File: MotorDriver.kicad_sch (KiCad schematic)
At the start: 93 parts, among them J1 Screw_Terminal_01x02, J2 Screw_Terminal_01x02, J3 Screw_Terminal_01x02, J4 Conn_01x07_Pin, J5 Conn_01x05_Pin, Q1 PMOS, U1 L298N, U2 INA226, U3 INA226, U4 INA226, U5 AP63205WU, U6 LM393, U7 AP2112K-3.3

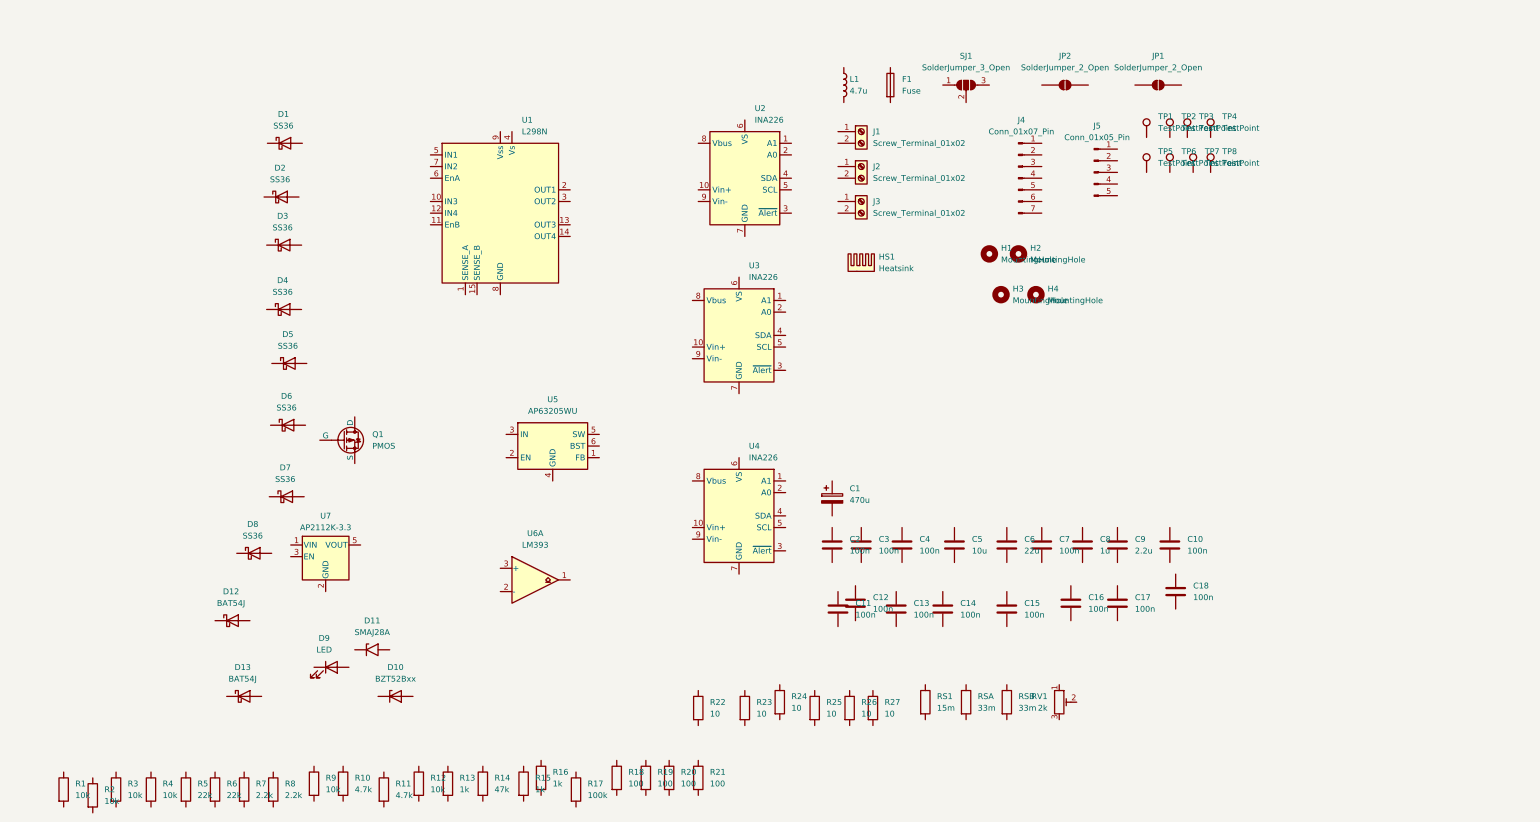
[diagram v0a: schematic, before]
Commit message: schematic update
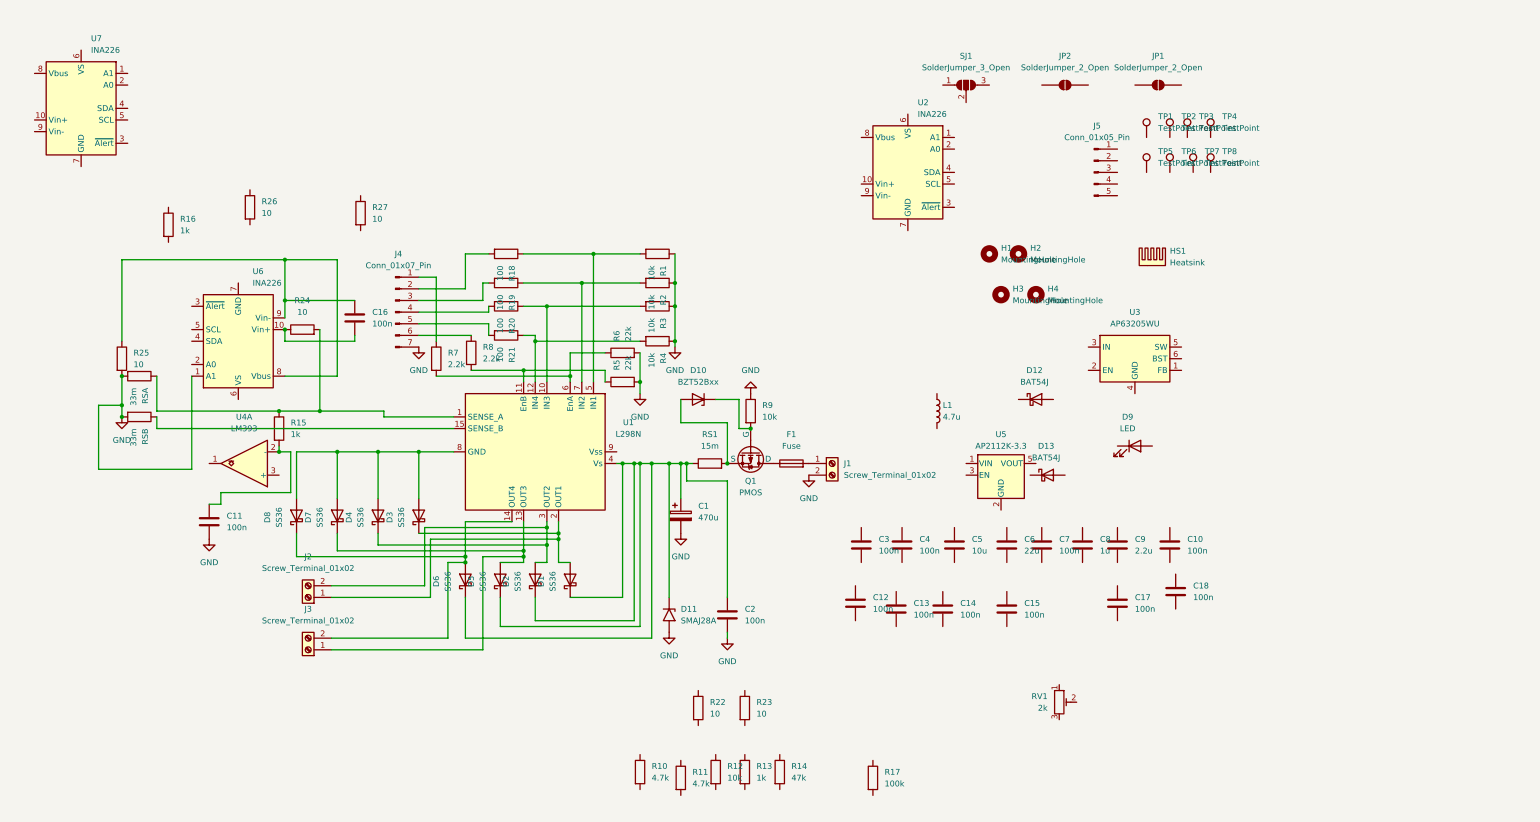
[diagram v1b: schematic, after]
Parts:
- renumbered U5 to U3, U6 to U4, U7 to U5, U4 to U6, U3 to U7
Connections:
- net at R20.1: now also R3.2, U1.10 (IN3)
- net at R20.2: now also J4.4 (Pin_4)
- net at J4.1 (Pin_1): now also R7.1
- net at J4.2 (Pin_2): now also R18.2
- net at J4.3 (Pin_3): now also R19.2
- net at J4.5 (Pin_5): now also R21.2
- net at J4.6 (Pin_6): now also R8.1
- net GND: now reaches J4.7 (Pin_7)
- net GND: now also C1.2, C11.2, C2.2, D11.2 (A2), J1.2 (Pin_2), R1.1, R2.1, R25.2, R3.1, R4.1, R5.2, R6.2, R9.1, RSA.2, RSB.2, U6.1 (A1)
- net at D10.1 (K): now also Q1.2 (G), R9.2
- net at D10.2 (A): now also Q1.3 (S), RS1.2
- net at C1.1: now also C2.1, D1.1 (K), D11.1 (A1), D2.1 (K), D5.1 (K), D6.1 (K), RS1.1, U1.4 (Vs)
- net at R8.2: now also R5.1, U1.11 (EnB)
- net at U1.1 (SENSE_A): now also R15.1, R24.2, RSA.1
- net at U1.12 (IN4): now also R21.1, R4.2
- net at U1.13 (OUT3): now also D5.2 (A), D7.1 (K), J3.1 (Pin_1)
- net at U1.14 (OUT4): now also D6.2 (A), D8.1 (K), J3.2 (Pin_2)
- net at U1.15 (SENSE_B): now also RSB.1
- net at U1.2 (OUT1): now also D1.2 (A), D3.1 (K), J2.1 (Pin_1)
- net at U1.3 (OUT2): now also D2.2 (A), D4.1 (K), J2.2 (Pin_2)
- net at U1.5 (IN1): now also R1.2, R18.1
- net at U1.6 (EnA): now also R6.1, R7.2
- net at U1.7 (IN2): now also R19.1, R2.2
- net at U1.8 (GND): now also D3.2 (A), D4.2 (A), D7.2 (A), D8.2 (A)
- net at U6.10 (Vin+): now also C16.2, R24.1
- net at U6.8 (Vbus): now also C16.1, R25.1, U6.9 (Vin-)
- net at Q1.1 (D): now also F1.1
- net at J1.1 (Pin_1): now also F1.2
- net at C11.1: now also R15.2, U4.2 (-)
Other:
- moved on the sheet: C1, C11, C16, C2, D1, D10, D12, D13, D5, D6, D7, D8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

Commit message: final schematic
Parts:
- removed JP1, JP2: SolderJumper_2_Open, symbol Jumper:SolderJumper_2_Open
- added JP1, JP2: SolderJumper_2_Bridged, symbol Jumper:SolderJumper_2_Bridged
- added unit 2 of U4
- added unit 3 of U4
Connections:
- net GND: now also C10.2, C12.2, C13.1, C15.2, C17.2, C3.2, C4.2, C5.2, C6.2, C8.1, C9.2, D9.1 (K), J5.5 (Pin_5), R27.2, RV1.3, TP2.1, U2.1 (A1), U2.2 (A0), U2.7 (GND), U3.4 (GND), U5.2 (GND), U6.7 (GND), U7.1 (A1), U7.7 (GND), U4.4 (V-)
- net at C12.1: now also R16.2, U4.6 (-)
- net at C18.1: now also R27.1, U7.8 (Vbus), U7.9 (Vin-)
- net at C18.2: now also R26.1, U7.10 (Vin+)
- net at U2.10 (Vin+): now also C14.1, R22.1
- net at U2.3 (~{Alert}): now also J5.3 (Pin_3), R12.1, U6.3 (~{Alert}), U7.3 (~{Alert})
- net at U2.4 (SDA): now also C16.1, J5.1 (Pin_1), R25.1, U6.4 (SDA), U6.8 (Vbus), U6.9 (Vin-), U7.2 (A0), U7.4 (SDA), JP1.1 (A)
- net at U2.5 (SCL): now also J5.2 (Pin_2), U6.5 (SCL), U7.5 (SCL), JP2.1 (A)
- net at U2.6 (VS): now also C10.1, C15.1, C17.1, C4.1, J5.4 (Pin_4), R10.2, R11.2, R12.2, SJ1.2 (C), U6.2 (A0), U6.6 (VS), U7.6 (VS), U4.8 (V+)
- net at U2.8 (Vbus): now also C1.1, C2.1, C5.1, D1.1 (K), D11.1 (A1), D2.1 (K), D5.1 (K), D6.1 (K), R17.1, R23.1, RS1.1, TP1.1, U1.4 (Vs), U3.3 (IN)
- net at U2.9 (Vin-): now also C14.2, R23.2
- net at D10.2 (A), Q1.3 (S), RS1.2: now also R22.2
- net at R5.1, R8.2, U1.11 (EnB): now also D13.1 (K)
- net at R15.1, R24.2, RSA.1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: now also TP5.1
- net at D5.2 (A), D7.1 (K), J3.1 (Pin_1)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: now also D2.2 (A), D4.1 (K), J2.2 (Pin_2), TP8.1, U1.3 (OUT2)
- net at RSB.1, U1.15 (SENSE_B): now also R16.1, R26.2, TP6.1
- net at D1.2 (A), D3.1 (K), J2.1 (Pin_1)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: now also TP7.1
- net at R6.1, R7.2, U1.6 (EnA): now also D12.1 (K)
- net +5V: now reaches U1.9 (Vss)
- net +5V: now also C3.1, C6.1, C8.2, L1.2, R13.1, SJ1.1 (A), TP3.1, U3.1 (FB), U5.1 (VIN), U5.3 (EN)
- net at D9.2 (A): now also R13.2
- net at R17.2: now also U3.2 (EN)
- net at D12.2 (A): now also U4.1
- net +3.3V: now reaches TP4.1
- net +3.3V: now also C9.1, R14.2, SJ1.3 (B), U5.5 (VOUT)
- net at R11.1: now also JP2.2 (B)
- net at U3.5 (SW): now also C7.1, L1.1
- net at U3.6 (BST): now also C7.2
- net at C13.2: now also R14.1, RV1.1, RV1.2, U4.3 (+), U4.5 (+)
- net at D13.2 (A): now also U4.7
- net at R10.1: now also JP1.2 (B)
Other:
- moved on the sheet: C1, C10, C11, C12, C13, C14, C15, C16, C17, C18, C2, C3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

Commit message: footprints assigned
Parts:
- removed HS1: Heatsink, symbol Mechanical:Heatsink
- C1: footprint (none) -> Capacitor_THT:CP_Radial_D10.0mm_P5.00mm_P7.50mm
- C10, C11, C12, C13, C14, C15, C16, C17, C18, C2, C3, C4, C7, C8, C9: footprint (none) -> Capacitor_SMD:C_0805_2012Metric_Pad1.18x1.45mm_HandSolder
- C5, C6: footprint (none) -> Capacitor_SMD:C_1206_3216Metric_Pad1.33x1.80mm_HandSolder
- D9: footprint (none) -> LED_SMD:LED_0805_2012Metric_Pad1.15x1.40mm_HandSolder
- F1: footprint (none) -> Fuse:Fuseholder_Cylinder-5x20mm_Schurter_0031_8201_Horizontal_Open
- H1, H2, H3, H4: footprint (none) -> MountingHole:MountingHole_3.2mm_M3
- J1, J2, J3: footprint (none) -> TerminalBlock_Phoenix:TerminalBlock_Phoenix_MKDS-1,5-2-5.08_1x02_P5.08mm_Horizontal
- J4: footprint (none) -> Connector_PinHeader_2.54mm:PinHeader_1x07_P2.54mm_Vertical
- J5: footprint (none) -> Connector_PinHeader_2.54mm:PinHeader_1x05_P2.54mm_Vertical
- JP1, JP2: footprint (none) -> Jumper:SolderJumper-2_P1.3mm_Bridged_RoundedPad1.0x1.5mm
- L1: footprint (none) -> Inductor_SMD:L_Bourns_SRN6045TA
- Q1: footprint (none) -> Package_TO_SOT_SMD:TO-252-2
- R1, R10, R11, R12, R13, R14, R15, R16, R17, R18, R19, R2, R20, R21, R22, R23, R24, R25, R26, R27, R3, R4, R5, R6, R7, R8, R9: footprint (none) -> Resistor_SMD:R_0603_1608Metric_Pad0.98x0.95mm_HandSolder
- RS1: footprint (none) -> Resistor_SMD:R_2512_6332Metric_Pad1.40x3.35mm_HandSolder
- RSA1: renamed from RSA; footprint (none) -> Resistor_SMD:R_2512_6332Metric_Pad1.40x3.35mm_HandSolder
- RSB1: renamed from RSB; footprint (none) -> Resistor_SMD:R_2512_6332Metric_Pad1.40x3.35mm_HandSolder
- RV1: footprint (none) -> Potentiometer_THT:Potentiometer_Bourns_3296W_Vertical
- SJ1: footprint (none) -> Jumper:SolderJumper-3_P1.3mm_Open_RoundedPad1.0x1.5mm
- TP1, TP2, TP3, TP4, TP5, TP6, TP7, TP8: footprint (none) -> TestPoint:TestPoint_Pad_D1.5mm
- U4: footprint (none) -> Package_SO:SOIC-8_3.9x4.9mm_P1.27mm
